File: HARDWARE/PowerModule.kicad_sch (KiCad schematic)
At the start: 11 parts, among them U3 LM1117-3.3, U4 LM1117-3.3, U5 LM1117-3.3

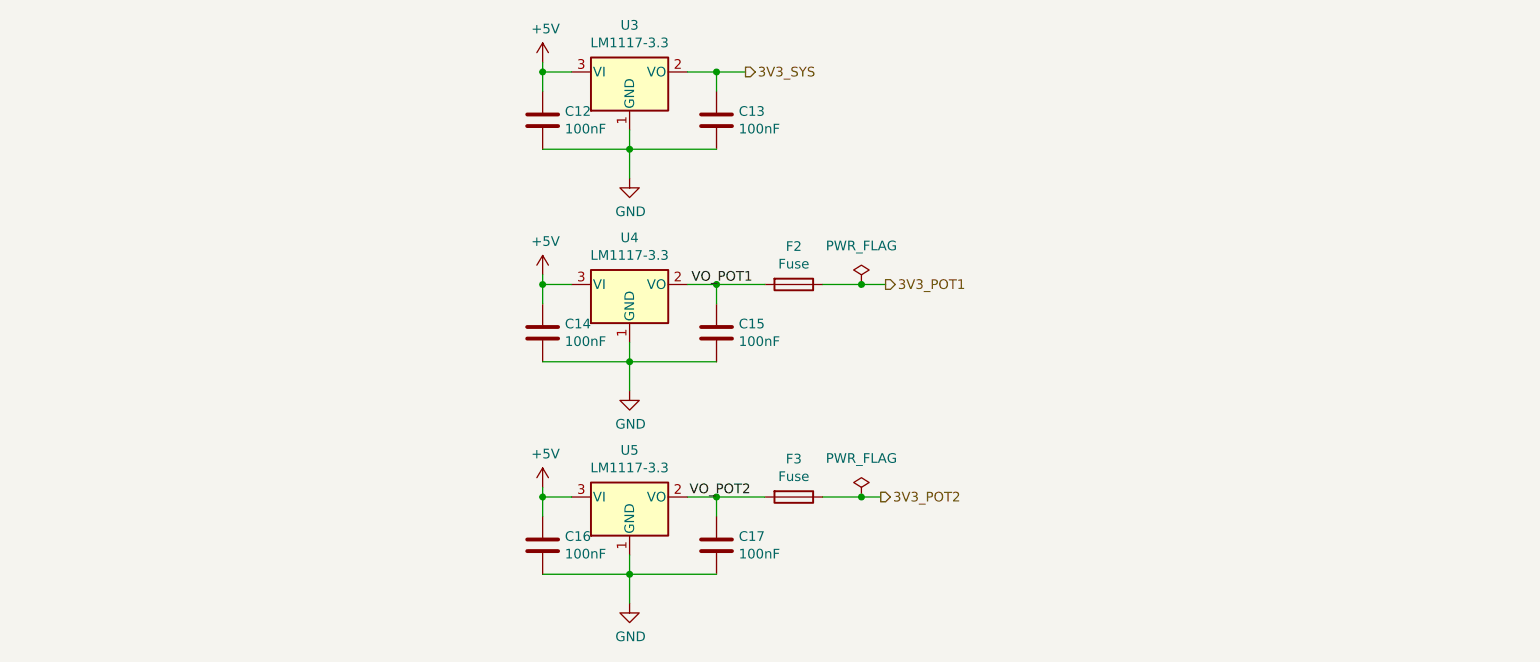
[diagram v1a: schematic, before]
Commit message: Align components on the PCB
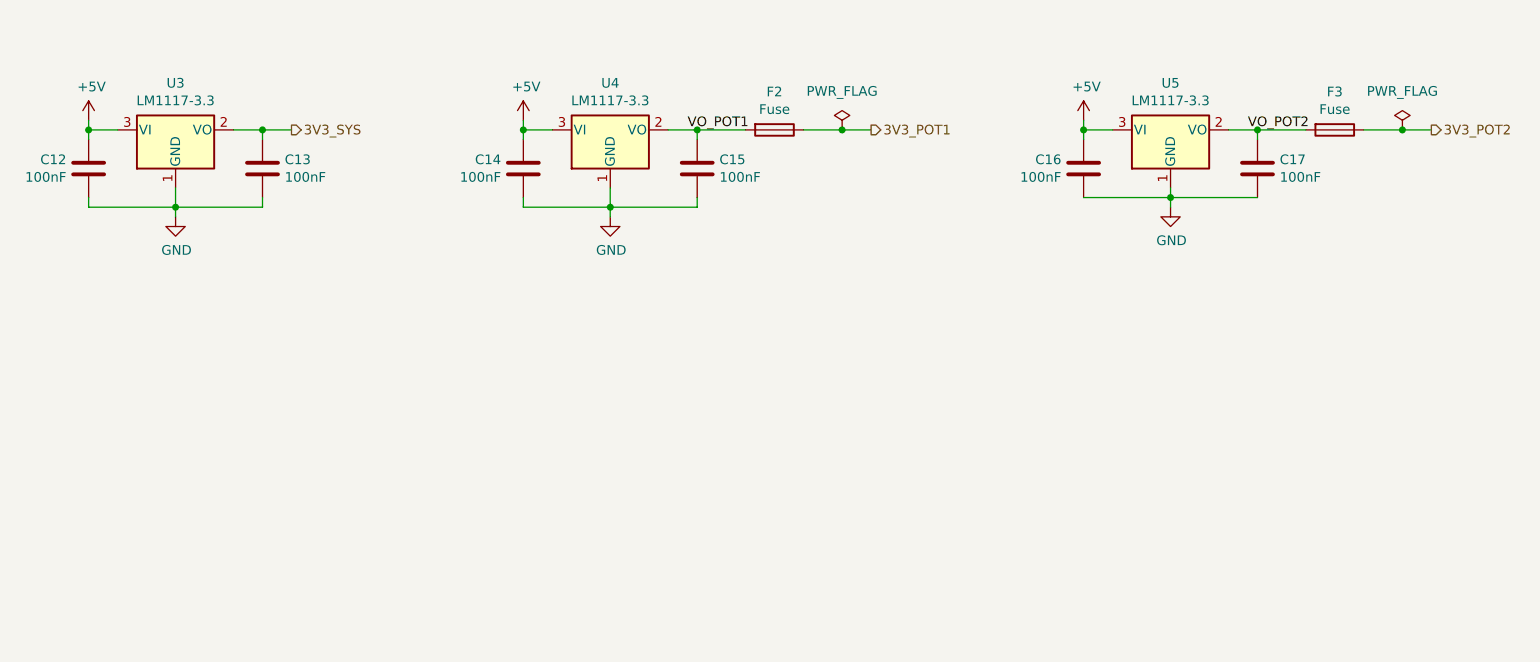
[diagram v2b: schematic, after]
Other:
- company: (none) -> PUT Motorsport
- moved on the sheet: C12, C13, C14, C15, C16, C17, F2, F3, U3, U4, U5

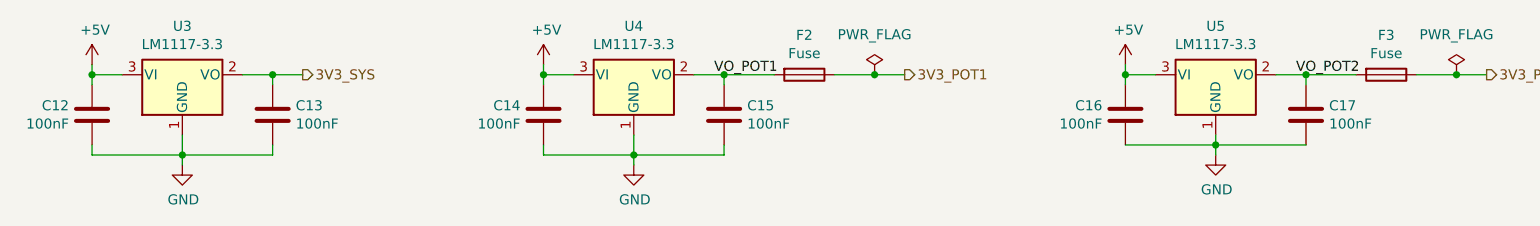
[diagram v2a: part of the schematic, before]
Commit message: Route PCB tracks
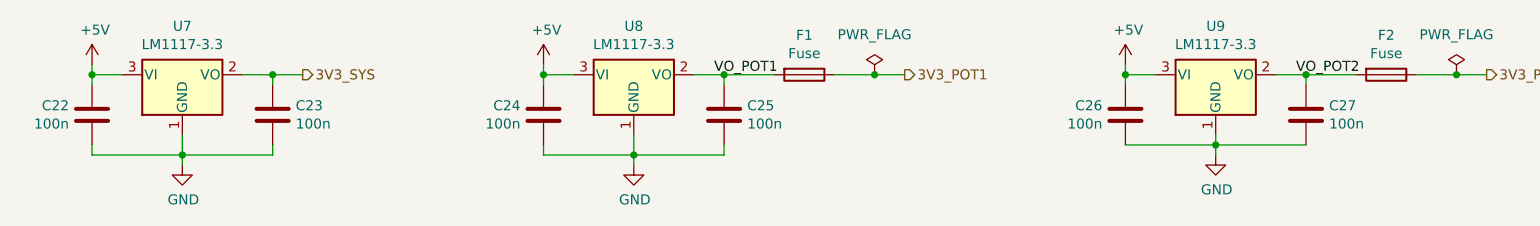
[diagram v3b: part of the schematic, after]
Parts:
- C22: renamed from C12; value 100nF -> 100n
- C23: renamed from C13; value 100nF -> 100n
- C24: renamed from C14; value 100nF -> 100n
- C25: renamed from C15; value 100nF -> 100n
- C26: renamed from C16; value 100nF -> 100n
- C27: renamed from C17; value 100nF -> 100n
- renumbered F2 to F1, F3 to F2, U3 to U7, U4 to U8, U5 to U9
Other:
- company: PUT Motorsport -> S. Sambor
- title: (none) -> Power for Potentiometers
